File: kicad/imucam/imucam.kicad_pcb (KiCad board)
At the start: 4 copper layers, 164 parts, among them J1 JTAG, J2 EXTCAM, J3 FSYNC_SEL, J4 NUCLEO_CN8, J5 NUCLEO_CN7, J6 NUCLEO_CN9, J7 NUCLEO_CN10, J8 HDMI, Q1 BSS214NW, Q2 BSS214NW, Q3 BSS214NW, Q4 BSS214NW, Q5 BSS214NW, Q6 BSS214NW, U1 TLV73310PDBVT, U10 PTN3366, U2 LIFCL-17-xSG72, U3 AT25SF081-SSHD-X, U4 MIC5365-2.8YD5, U5 AR0330CM1C00, U6 ICM20948, U7 TPS562200, U8 TPS562200, U9 AP2331, X1 ECS-2520MV-xxx-xx

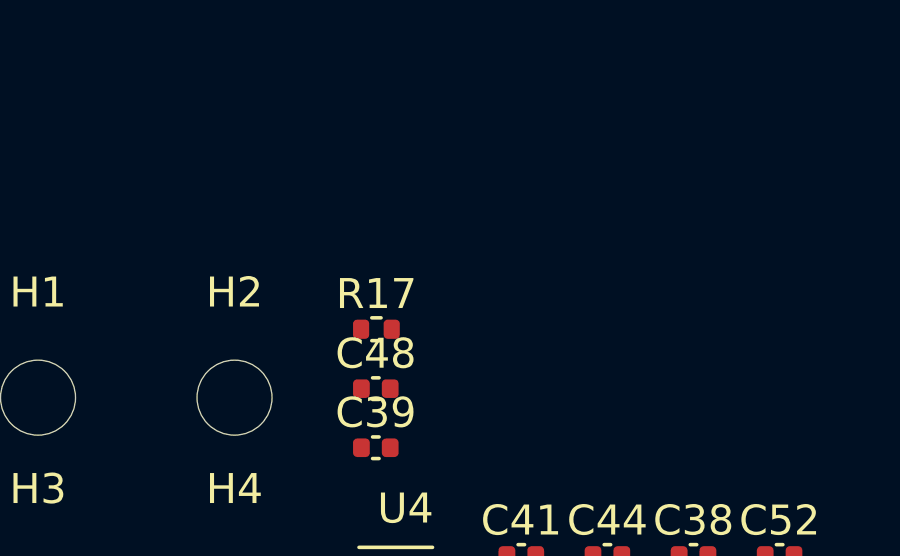
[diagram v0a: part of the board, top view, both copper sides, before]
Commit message: Added 3.3v power LED
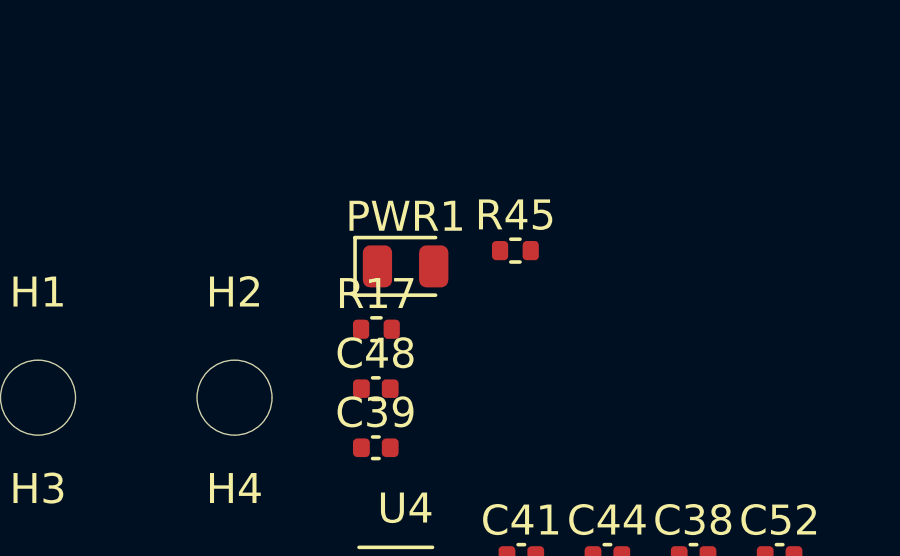
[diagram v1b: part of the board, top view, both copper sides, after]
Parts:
- added PWR1: RED, LED_SMD:LED_0805_2012Metric, F.Cu at (-37.3, -39.4)
- added R45: 1k, Resistor_SMD:R_0402_1005Metric, F.Cu at (-33.6, -39.9)

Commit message: More work on PCB
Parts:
- removed H1, H2, H3, H4: MountingHole, MountingHole:MountingHole_2.5mm
- removed J3: FSYNC_SEL, Connector_PinHeader_2.54mm:PinHeader_1x03_P2.54mm_Vertical
- added JP1: SolderJumper_3_Open, Jumper:SolderJumper-3_P1.3mm_Open_Pad1.0x1.5mm, F.Cu at (40.7, 40.1)
- R14, R2, R3, R4: value 1k -> 100
- moved R40 135.4 mm to (48.6, 68.8), turned to 90 degrees
- moved R44 134.4 mm to (49.7, 68.8), turned to 270 degrees
- moved R41 131.0 mm to (46.4, 68.8), turned to 90 degrees
- moved R39 130.8 mm to (45.4, 68.8), turned to 90 degrees
- moved R38 129.4 mm to (44.3, 68.8), turned to 90 degrees
- moved R42 124.4 mm to (47.5, 68.8), turned to 90 degrees
- moved R17 117.8 mm to (42.8, 48.2)
- moved R36 116.7 mm to (38.7, 15.4), turned to 180 degrees
- moved R37 105.8 mm to (38.7, 16.4), turned to 180 degrees
- moved R18 105.2 mm to (42.5, 40.6), turned to 270 degrees
- moved C68 96.0 mm to (18.0, 23.7), turned to 270 degrees
- moved U9 93.3 mm to (16.1, 18.5)
- moved U4 92.9 mm to (35.4, 29.5), turned to 180 degrees
- moved C67 91.1 mm to (19.5, 23.7), turned to 270 degrees
- moved C53 86.8 mm to (37.9, 29.9), turned to 90 degrees
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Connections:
- net Net-(C66-Pad1) renamed /hdmi/5V_HDMI

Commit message: Switched FSYNC to use TRIGGER, lots of PCB work
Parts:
- removed JP1: SolderJumper_3_Open, Jumper:SolderJumper-3_P1.3mm_Open_Pad1.0x1.5mm
- removed the R18 at (42.5, 40.6)
- removed the R43 at (13.0, 24.6)
- added H1: M12Lens, imucam:M12_Lens_20mm, F.Cu at (24.1, 28.4)
- added H2: EXTCAM, imucam:Arducam_module_40mm, F.Cu at (24.8, 47.7)
- added R32: 10k, Resistor_SMD:R_0402_1005Metric, F.Cu at (-24.7, 32.7)
- added R37: 10k, Resistor_SMD:R_0402_1005Metric, F.Cu at (-21.8, 32.7)
- added R45: 12.4k 1%, Resistor_SMD:R_0402_1005Metric, F.Cu at (37.2, 57.8)
- C38, C39, C40, C41, C42, C43, C44, C45, C46, C47, C48, C49, C50, C51: moved to B.Cu
- J2: moved to F.Cu
- moved C22 216.2 mm to (-184.1, 58.5)
- moved C23 216.2 mm to (-189.2, 58.5)
- moved D1 216.2 mm to (-207.0, -17.7)
- moved R10 216.2 mm to (-204.4, 30.6)
- moved R11 216.2 mm to (-204.4, 29.3)
- moved R12 216.2 mm to (-204.4, 31.9)
- moved R13 216.2 mm to (-204.4, 34.4)
- moved R16 216.2 mm to (-204.4, 33.1)
- moved L1 156.3 mm to (9.40, 66.5)
- moved U7 156.3 mm to (14.2, 66.4)
- moved L2 144.3 mm to (-48.0, 89.0)
- moved C57 144.2 mm to (-46.6, 104.4)
- moved C58 144.2 mm to (-44.5, 99.1)
- moved C59 144.2 mm to (-49.5, 106.3)
- moved C60 144.2 mm to (-48.9, 102.1)
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- renumbered J4 to J3, J5 to J4, J6 to J5, J7 to J6, J8 to J7, R19 to R18, R20 to R19, R21 to R20, R22 to R21, R23 to R22, R24 to R23, R25 to R24, R26 to R25, R27 to R26, R28 to R27, R29 to R28, R30 to R29, R31 to R30, R32 to R31, R45 to R36, R36 to R38, R37 to R39, R38 to R40, R39 to R41, R40 to R42, R41 to R43, R42 to R44, R44 to R46, PWR1 to STM_LED4
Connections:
- J5 pad 18: (no net) -> CAM_TRIGGER
- J5 pad 20: CAM_FLASH -> (no net)
- U5 pad 3: CAM_FLASH -> (no net)
- U5 pad 35: CAM_SHUTTER -> (no net)
- U5 pad 36: GND -> CAM_TRIGGER
- U6 pad 11: Net-(JP1-Pad2) -> CAM_TRIGGER
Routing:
- net +1V8: track 0.00 -> 0.81 mm
- net GND: track 0.00 -> 0.06 mm, vias 0 -> 18
- net +3V3: vias 0 -> 1
- added copper zone on In2.Cu, net +1V8
- added copper zone on In1.Cu, net GND
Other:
- board outline added: 52.3 x 76.2 mm

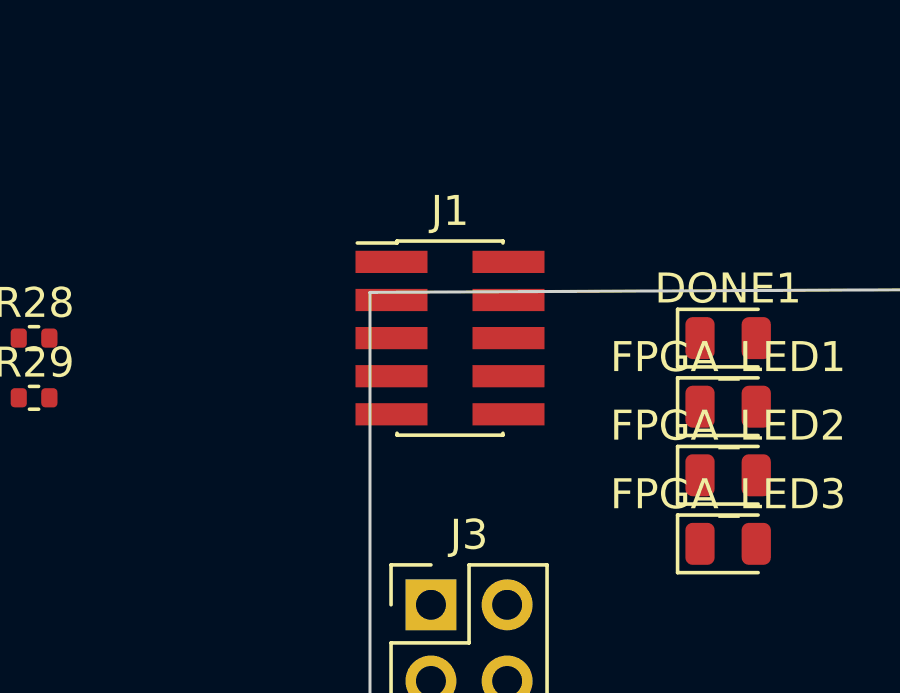
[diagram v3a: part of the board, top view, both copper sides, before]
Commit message: Through-hole JTAG
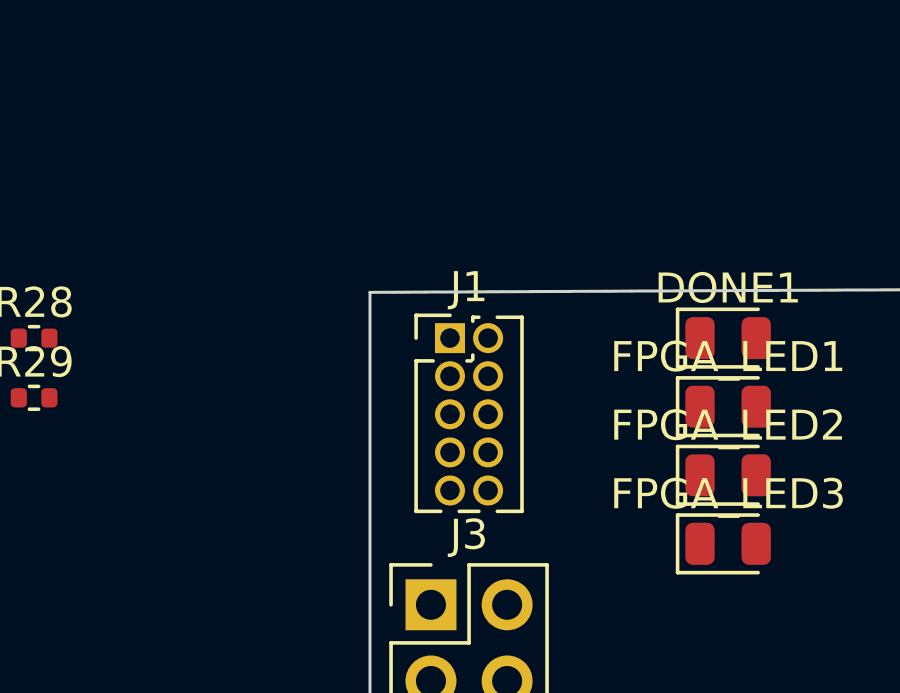
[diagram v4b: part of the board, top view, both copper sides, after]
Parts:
- J1: footprint Connector_PinHeader_1.27mm:PinHeader_2x05_P1.27mm_Vertical_SMD -> Connector_PinHeader_1.27mm:PinHeader_2x05_P1.27mm_Vertical
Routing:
- net GND: vias 18 -> 19
- net +3V3: vias 1 -> 0
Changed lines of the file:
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@@
     (add_net SDA_3V3)
   )
+  (module Connector_PinHeader_1.27mm:PinHeader_2x05_P1.27mm_Vertical (layer F.Cu)
+    (at 0.635 3.81)
+    (descr "Through hole straight pin header, 2x05, 1.27mm pitch, double rows")
+    (tags "Through hole pin header THT 2x05 1.27mm double row")
+    (fp_text reference J1 (at 0.635 -1.695) (layer F.SilkS)
+      (effects (font (size 1 1) (thickness 0.15)))
+    )
+    (fp_text value JTAG (at 0.635 6.775) (layer F.Fab)
+      (effects (font (size 1 1) (thickness 0.15)))
+    )
+    (fp_text user %R (at 0.635 2.54 90) (layer F.Fab)
+      (effects (font (size 1 1) (thickness 0.15)))
+    )
+    (fp_line (start -0.2175 -0.635) (end 2.34 -0.635) (layer F.Fab) (width 0.1))
+    (fp_line (start 2.34 -0.635) (end 2.34 5.715) (layer F.Fab) (width 0.1))
+    (fp_line (start 2.34 5.715) (end -1.07 5.715) (layer F.Fab) (width 0.1))
+    (fp_line (start -1.07 5.715) (end -1.07 0.2175) (layer F.Fab) (width 0.1))
+    (fp_line (start -1.07 0.2175) (end -0.2175 -0.635) (layer F.Fab) (width 0.1))
+    (fp_line (start -1.13 5.775) (end -0.30753 5.775) (layer F.SilkS) (width 0.12))
+    (fp_line (start 1.57753 5.775) (end 2.4 5.775) (layer F.SilkS) (width 0.12))
+    (fp_line (start 0.30753 5.775) (end 0.96247 5.775) (layer F.SilkS) (width 0.12))
+    (fp_line (start -1.13 0.76) (end -1.13 5.775) (layer F.SilkS) (width 0.12))
+    (fp_line (start 2.4 -0.695) (end 2.4 5.775) (layer F.SilkS) (width 0.12))
+    (fp_line (start -1.13 0.76) (end -0.563471 0.76) (layer F.SilkS) (width 0.12))
+    (fp_line (start 0.563471 0.76) (end 0.706529 0.76) (layer F.SilkS) (width 0.12))
+    (fp_line (start 0.76 0.706529) (end 0.76 0.563471) (layer F.SilkS) (width 0.12))
+    (fp_line (start 0.76 -0.563471) (end 0.76 -0.695) (layer F.SilkS) (width 0.12))
+    (fp_line (start 0.76 -0.695) (end 0.96247 -0.695) (layer F.SilkS) (width 0.12))
+    (fp_line (start 1.57753 -0.695) (end 2.4 -0.695) (layer F.SilkS) (width 0.12))
+    (fp_line (start -1.13 0) (end -1.13 -0.76) (layer F.SilkS) (width 0.12))
+    (fp_line (start -1.13 -0.76) (end 0 -0.76) (layer F.SilkS) (width 0.12))
+    (fp_line (start -1.6 -1.15) (end -1.6 6.25) (layer F.CrtYd) (width 0.05))
+    (fp_line (start -1.6 6.25) (end 2.85 6.25) (layer F.CrtYd) (width 0.05))
+    (fp_line (start 2.85 6.25) (end 2.85 -1.15) (layer F.CrtYd) (width 0.05))
+    (fp_line (start 2.85 -1.15) (end -1.6 -1.15) (layer F.CrtYd) (width 0.05))
+    (pad 10 thru_hole oval (at 1.27 5.08) (size 1 1) (drill 0.65) (layers *.Cu *.Mask)
+      (net 33 /FPGA/JTAG_RESET))
+    (pad 9 thru_hole oval (at 0 5.08) (size 1 1) (drill 0.65) (layers *.Cu *.Mask)
+      (net 1 GND))
+    (pad 8 thru_hole oval (at 1.27 3.81) (size 1 1) (drill 0.65) (layers *.Cu *.Mask)
+      (net 43 /FPGA/JTAG_TDI))
+    (pad 7 thru_hole oval (at 0 3.81) (size 1 1) (drill 0.65) (layers *.Cu *.Mask))
+    (pad 6 thru_hole oval (at 1.27 2.54) (size 1 1) (drill 0.65) (layers *.Cu *.Mask)
+      (net 44 /FPGA/JTAG_TDO))
+    (pad 5 thru_hole oval (at 0 2.54) (size 1 1) (drill 0.65) (layers *.Cu *.Mask)
+      (net 1 GND))
+    (pad 4 thru_hole oval (at 1.27 1.27) (size 1 1) (drill 0.65) (layers *.Cu *.Mask)
+      (net 45 /FPGA/JTAG_TCK))
+    (pad 3 thru_hole oval (at 0 1.27) (size 1 1) (drill 0.65) (layers *.Cu *.Mask)
+      (net 1 GND))
+    (pad 2 thru_hole oval (at 1.27 0) (size 1 1) (drill 0.65) (layers *.Cu *.Mask)
+      (net 46 /FPGA/JTAG_TMS))
+    (pad 1 thru_hole rect (at 0 0) (size 1 1) (drill 0.65) (layers *.Cu *.Mask)
+      (net 6 +3V3))
+    (model ${KISYS3DMOD}/Connector_PinHeader_1.27mm.3dshapes/PinHeader_2x05_P1.27mm_Vertical.wrl
+      (at (xyz 0 0 0))
+      (scale (xyz 1 1 1))
+      (rotate (xyz 0 0 0))
+    )
+  )
   (module Resistor_SMD:R_0402_1005Metric (layer F.Cu)
     (at -21.7915 32.7025)
@@
     )
   )
-  (module Connector_PinHeader_1.27mm:PinHeader_2x05_P1.27mm_Vertical_SMD (layer F.Cu)
-    (at 0.635 3.81)
-    (descr "surface-mounted straight pin header, 2x05, 1.27mm pitch, double rows")
-    (tags "Surface mounted pin header SMD 2x05 1.27mm double row")
-    (attr smd)
-    (fp_text reference J1 (at 0 -4.235) (layer F.SilkS)
-      (effects (font (size 1 1) (thickness 0.15)))
-    )
-    (fp_text value JTAG (at 0 4.235) (layer F.Fab)
-      (effects (font (size 1 1) (thickness 0.15)))
-    )
-    (fp_text user %R (at 0 0 90) (layer F.Fab)
-      (effects (font (size 1 1) (thickness 0.15)))
-    )
-    (fp_line (start 1.705 3.175) (end -1.705 3.175) (layer F.Fab) (width 0.1))
-    (fp_line (start -1.27 -3.175) (end 1.705 -3.175) (layer F.Fab) (width 0.1))
-    (fp_line (start -1.705 3.175) (end -1.705 -2.74) (layer F.Fab) (width 0.1))
-    (fp_line (start -1.705 -2.74) (end -1.27 -3.175) (layer F.Fab) (width 0.1))
-    (fp_line (start 1.705 -3.175) (end 1.705 3.175) (layer F.Fab) (width 0.1))
-    (fp_line (start -1.705 -2.74) (end -2.75 -2.74) (layer F.Fab) (width 0.1))
-    (fp_line (start -2.75 -2.74) (end -2.75 -2.34) (layer F.Fab) (width 0.1))
-    (fp_line (start -2.75 -2.34) (end -1.705 -2.34) (layer F.Fab) (width 0.1))
-    (fp_line (start 1.705 -2.74) (end 2.75 -2.74) (layer F.Fab) (width 0.1))
-    (fp_line (start 2.75 -2.74) (end 2.75 -2.34) (layer F.Fab) (width 0.1))
-    (fp_line (start 2.75 -2.34) (end 1.705 -2.34) (layer F.Fab) (width 0.1))
-    (fp_line (start -1.705 -1.47) (end -2.75 -1.47) (layer F.Fab) (width 0.1))
-    (fp_line (start -2.75 -1.47) (end -2.75 -1.07) (layer F.Fab) (width 0.1))
-    (fp_line (start -2.75 -1.07) (end -1.705 -1.07) (layer F.Fab) (width 0.1))
-    (fp_line (start 1.705 -1.47) (end 2.75 -1.47) (layer F.Fab) (width 0.1))
-    (fp_line (start 2.75 -1.47) (end 2.75 -1.07) (layer F.Fab) (width 0.1))
-    (fp_line (start 2.75 -1.07) (end 1.705 -1.07) (layer F.Fab) (width 0.1))
-    (fp_line (start -1.705 -0.2) (end -2.75 -0.2) (layer F.Fab) (width 0.1))
-    (fp_line (start -2.75 -0.2) (end -2.75 0.2) (layer F.Fab) (width 0.1))
-    (fp_line (start -2.75 0.2) (end -1.705 0.2) (layer F.Fab) (width 0.1))
-    (fp_line (start 1.705 -0.2) (end 2.75 -0.2) (layer F.Fab) (width 0.1))
-    (fp_line (start 2.75 -0.2) (end 2.75 0.2) (layer F.Fab) (width 0.1))
-    (fp_line (start 2.75 0.2) (end 1.705 0.2) (layer F.Fab) (width 0.1))
-    (fp_line (start -1.705 1.07) (end -2.75 1.07) (layer F.Fab) (width 0.1))
-    (fp_line (start -2.75 1.07) (end -2.75 1.47) (layer F.Fab) (width 0.1))
-    (fp_line (start -2.75 1.47) (end -1.705 1.47) (layer F.Fab) (width 0.1))
-    (fp_line (start 1.705 1.07) (end 2.75 1.07) (layer F.Fab) (width 0.1))
-    (fp_line (start 2.75 1.07) (end 2.75 1.47) (layer F.Fab) (width 0.1))
-    (fp_line (start 2.75 1.47) (end 1.705 1.47) (layer F.Fab) (width 0.1))
-    (fp_line (start -1.705 2.34) (end -2.75 2.34) (layer F.Fab) (width 0.1))
-    (fp_line (start -2.75 2.34) (end -2.75 2.74) (layer F.Fab) (width 0.1))
-    (fp_line (start -2.75 2.74) (end -1.705 2.74) (layer F.Fab) (width 0.1))
-    (fp_line (start 1.705 2.34) (end 2.75 2.34) (layer F.Fab) (width 0.1))
-    (fp_line (start 2.75 2.34) (end 2.75 2.74) (layer F.Fab) (width 0.1))
-    (fp_line (start 2.75 2.74) (end 1.705 2.74) (layer F.Fab) (width 0.1))
-    (fp_line (start -1.765 -3.235) (end 1.765 -3.235) (layer F.SilkS) (width 0.12))
-    (fp_line (start -1.765 3.235) (end 1.765 3.235) (layer F.SilkS) (width 0.12))
-    (fp_line (start -3.09 -3.17) (end -1.765 -3.17) (layer F.SilkS) (width 0.12))
-    (fp_line (start -1.765 -3.235) (end -1.765 -3.17) (layer F.SilkS) (width 0.12))
-    (fp_line (start 1.765 -3.235) (end 1.765 -3.17) (layer F.SilkS) (width 0.12))
-    (fp_line (start -1.765 3.17) (end -1.765 3.235) (layer F.SilkS) (width 0.12))
-    (fp_line (start 1.765 3.17) (end 1.765 3.235) (layer F.SilkS) (width 0.12))
-    (fp_line (start -4.3 -3.7) (end -4.3 3.7) (layer F.CrtYd) (width 0.05))
-    (fp_line (start -4.3 3.7) (end 4.3 3.7) (layer F.CrtYd) (width 0.05))
-    (fp_line (start 4.3 3.7) (end 4.3 -3.7) (layer F.CrtYd) (width 0.05))
-    (fp_line (start 4.3 -3.7) (end -4.3 -3.7) (layer F.CrtYd) (width 0.05))
-    (pad 10 smd rect (at 1.95 2.54) (size 2.4 0.74) (layers F.Cu F.Paste F.Mask)
-      (net 33 /FPGA/JTAG_RESET))
-    (pad 9 smd rect (at -1.95 2.54) (size 2.4 0.74) (layers F.Cu F.Paste F.Mask)
-      (net 1 GND))
-    (pad 8 smd rect (at 1.95 1.27) (size 2.4 0.74) (layers F.Cu F.Paste F.Mask)
-      (net 43 /FPGA/JTAG_TDI))
-    (pad 7 smd rect (at -1.95 1.27) (size 2.4 0.74) (layers F.Cu F.Paste F.Mask))
-    (pad 6 smd rect (at 1.95 0) (size 2.4 0.74) (layers F.Cu F.Paste F.Mask)
-      (net 44 /FPGA/JTAG_TDO))
-    (pad 5 smd rect (at -1.95 0) (size 2.4 0.74) (layers F.Cu F.Paste F.Mask)
-      (net 1 GND))
-    (pad 4 smd rect (at 1.95 -1.27) (size 2.4 0.74) (layers F.Cu F.Paste F.Mask)
-      (net 45 /FPGA/JTAG_TCK))
-    (pad 3 smd rect (at -1.95 -1.27) (size 2.4 0.74) (layers F.Cu F.Paste F.Mask)
-      (net 1 GND))
-    (pad 2 smd rect (at 1.95 -2.54) (size 2.4 0.74) (layers F.Cu F.Paste F.Mask)
-      (net 46 /FPGA/JTAG_TMS))
-    (pad 1 smd rect (at -1.95 -2.54) (size 2.4 0.74) (layers F.Cu F.Paste F.Mask)
-      (net 6 +3V3))
-    (model ${KISYS3DMOD}/Connector_PinHeader_1.27mm.3dshapes/PinHeader_2x05_P1.27mm_Vertical_SMD.wrl
-      (at (xyz 0 0 0))
-      (scale (xyz 1 1 1))
-      (rotate (xyz 0 0 0))
-    )
-  )
   (module imucam:Arducam_module_40mm (layer F.Cu)
     (at 24.8285 47.6885 180)
@@
   (gr_line (start -2.032 78.232) (end -2.032 2.286) (layer Edge.Cuts) (width 0.1))
   (gr_line (start 50.292 2.032) (end -2.032 2.286) (layer Edge.Cuts) (width 0.1))
-  (via (at 38.989 50.4825) (size 0.4572) (drill 0.254) (layers F.Cu B.Cu) (net 6))
+  (via (at 38.989 50.4825) (size 0.4572) (drill 0.254) (layers F.Cu B.Cu) (net 1))
   (via (at 37.719 53.7845) (size 0.4572) (drill 0.254) (layers F.Cu B.Cu) (net 1))
   (via (at 36.3855 58.42) (size 0.4572) (drill 0.254) (layers F.Cu B.Cu) (net 1))

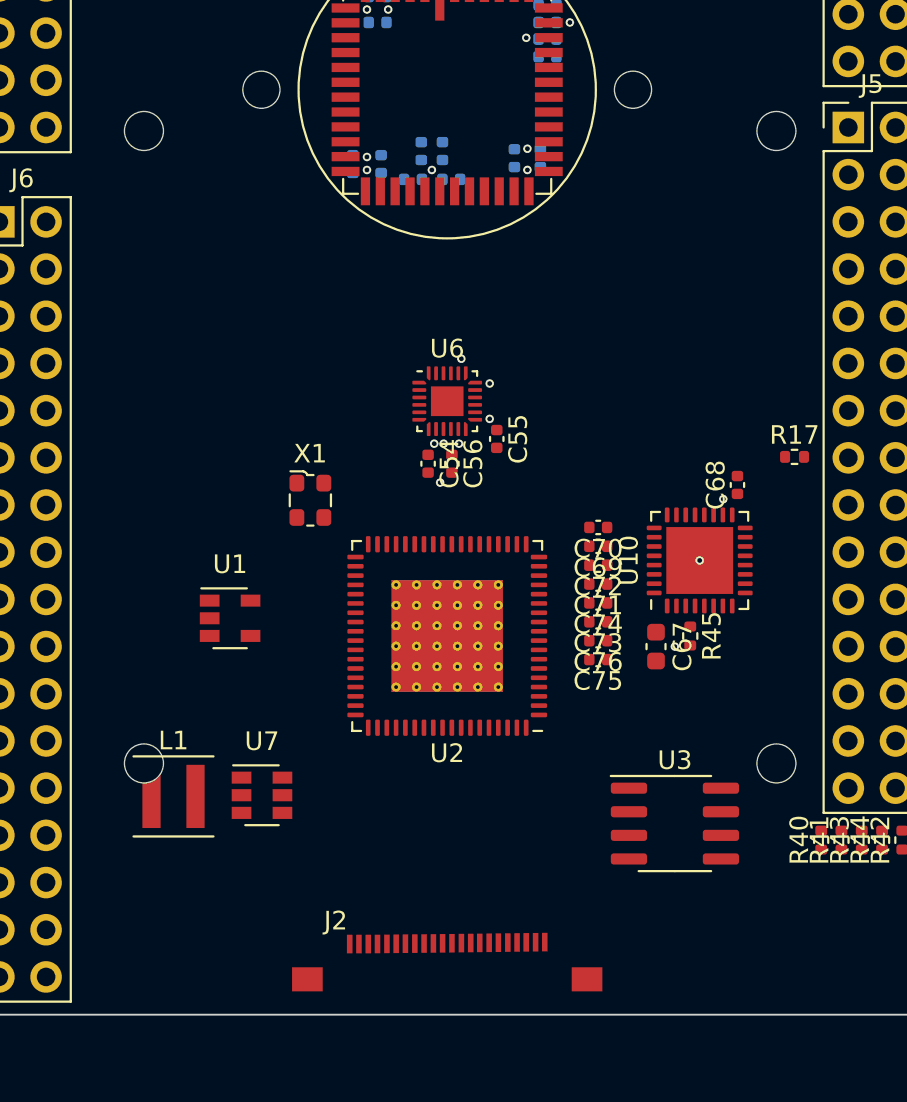
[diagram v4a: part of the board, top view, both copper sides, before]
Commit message: More PCB work, began current sense
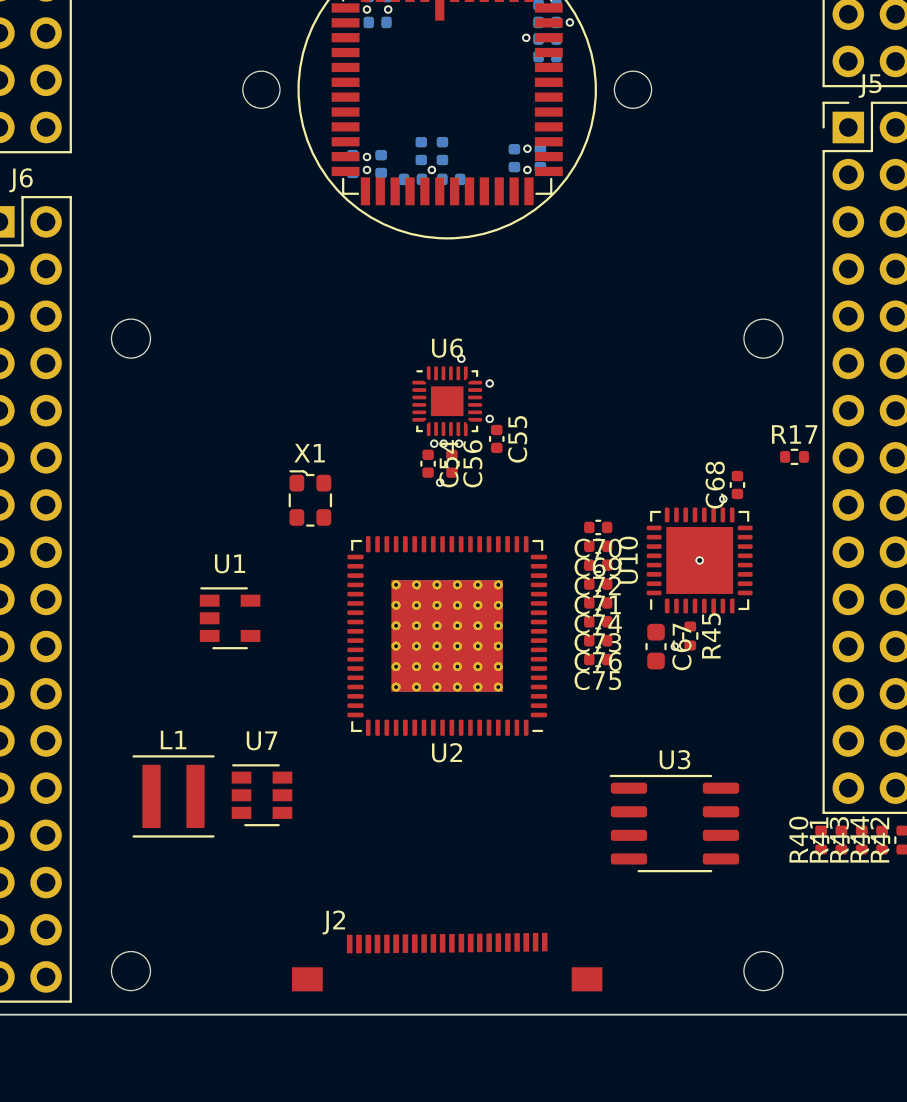
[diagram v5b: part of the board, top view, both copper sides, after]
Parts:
- moved H2 11.2 mm to (24.1, 58.9)
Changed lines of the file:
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@@
   )
   (module imucam:Arducam_module_40mm (layer F.Cu)
-    (at 24.8285 47.6885 180)
+    (at 24.13 58.8645 180)
     (fp_text reference H2 (at -10.75 21) (layer F.SilkS) hide
       (effects (font (size 1 1) (thickness 0.15)))
